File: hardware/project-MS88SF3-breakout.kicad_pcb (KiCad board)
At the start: 4 copper layers, 22.9 x 50.8 mm, 27 parts, among them J1 Conn_02x05_Odd_Even, J2 S2B-PH-SM4-TB(LF)(SN), J3 USB4105-GF-A, J4 Conn_01x12_Pin, J5 Conn_01x16_Pin, SW1 PTS810_SJM_250_SMTR_LFS, U1 MS88SF3_NRF52840

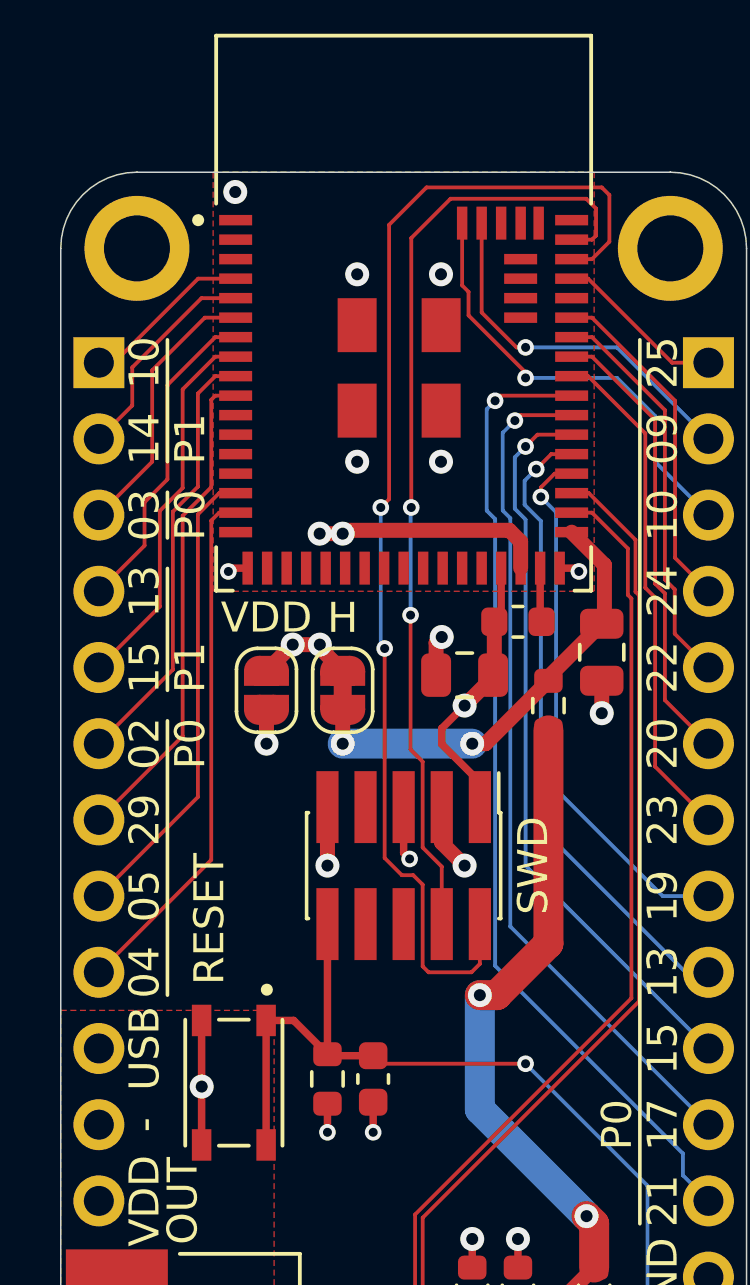
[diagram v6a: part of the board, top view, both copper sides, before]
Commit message: Route all nets
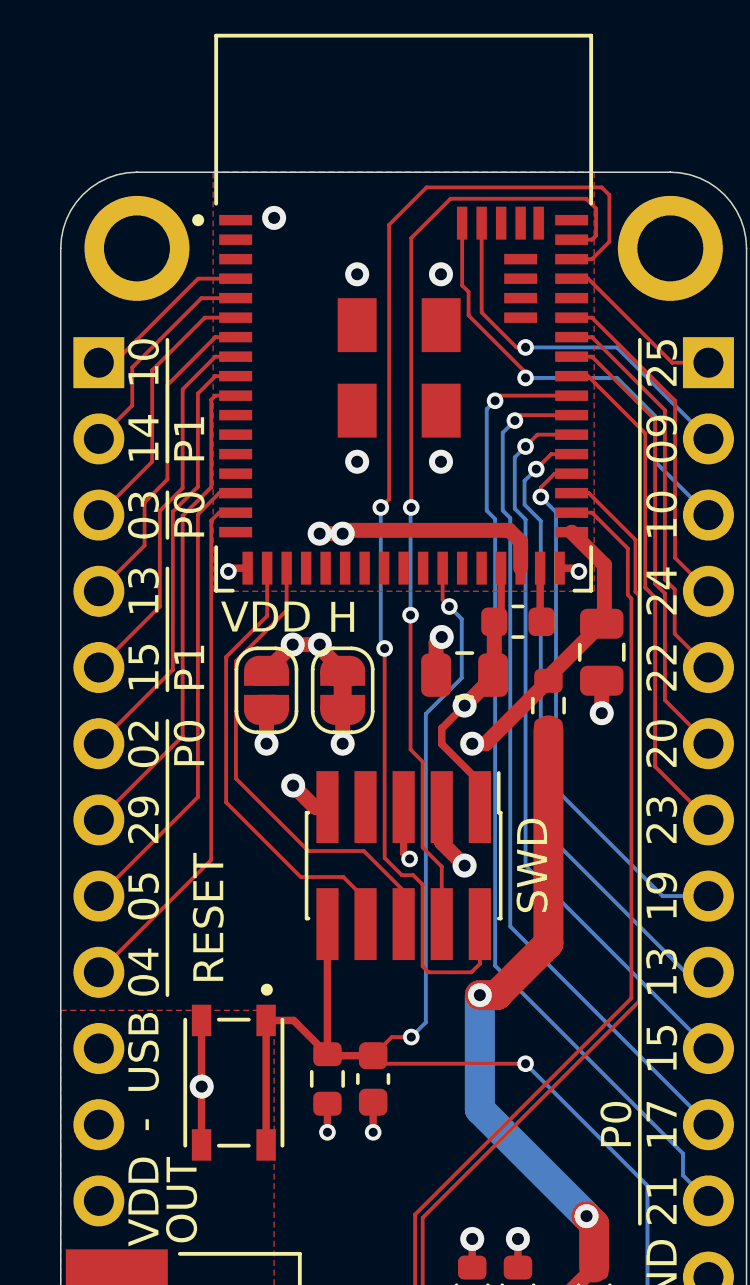
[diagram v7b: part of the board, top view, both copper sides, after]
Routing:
- net /RESET: track 35.0 -> 53.1 mm, vias 1 -> 3
- net /TX: track 0.00 -> 16.0 mm
- net /RX: track 0.00 -> 15.2 mm
- net GND: track 28.8 -> 28.2 mm
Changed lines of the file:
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@@
 	)
 	(gr_text "USB"
-		(at 38.862 109.982 90)
+		(at 38.862 110.109 90)
 		(layer "F.SilkS")
 		(effects
@@
 		(end 49.784048 99.822)
 		(width 1)
-		(layer "B.Cu")
+		(layer "In2.Cu")
 		(net 5)
 	)
@@
 	)
 	(segment
-		(start 44.958 101.936)
-		(end 44.958 103.886)
-		(width 0.5)
-		(layer "F.Cu")
-		(net 7)
-	)
-	(segment
 		(start 43.753 125.547)
 		(end 43.178 126.122)
@@
 	)
 	(segment
+		(start 44.958 101.936)
+		(end 44.532 101.936)
+		(width 0.5)
+		(layer "F.Cu")
+		(net 7)
+	)
+	(segment
 		(start 53.02 122.936)
 		(end 53.02 124.018)
@@
 	)
 	(segment
+		(start 44.532 101.936)
+		(end 43.815 101.219)
+		(width 0.5)
+		(layer "F.Cu")
+		(net 7)
+	)
+	(segment
 		(start 37.938 124.127)
 		(end 37.938 122.844)
@@
 	(via
 		(at 48.768 96.266)
+		(size 0.8)
+		(drill 0.4)
+		(layers "F.Cu" "B.Cu")
+		(net 7)
+	)
+	(via
+		(at 43.815 101.219)
 		(size 0.8)
 		(drill 0.4)
@@
 	)
 	(via
-		(at 41.8846 81.4324)
-		(size 0.8)
-		(drill 0.4)
-		(layers "F.Cu" "B.Cu")
-		(net 7)
-	)
-	(via
 		(at 48.7426 90.424)
 		(size 0.8)
@@
 	)
 	(via
-		(at 44.958 103.886)
-		(size 0.8)
-		(drill 0.4)
-		(layers "F.Cu" "B.Cu")
-		(net 7)
-	)
-	(via
 		(at 45.9486 90.424)
 		(size 0.8)
@@
 	)
 	(via
+		(at 43.18 82.296)
+		(size 0.8)
+		(drill 0.4)
+		(layers "F.Cu" "B.Cu")
+		(free yes)
+		(net 7)
+	)
+	(via
 		(at 38.1 122.682)
 		(size 0.8)
@@
 	)
 	(segment
+		(start 46.228 105.006)
+		(end 46.228 105.836)
+		(width 0.127)
+		(layer "F.Cu")
+		(net 16)
+	)
+	(segment
+		(start 41.5805 96.934795)
+		(end 41.5805 101.7785)
+		(width 0.127)
+		(layer "F.Cu")
+		(net 16)
+	)
+	(segment
+		(start 45.489 104.267)
+		(end 46.228 105.006)
+		(width 0.127)
+		(layer "F.Cu")
+		(net 16)
+	)
+	(segment
+		(start 44.069 104.267)
+		(end 45.489 104.267)
+		(width 0.127)
+		(layer "F.Cu")
+		(net 16)
+	)
+	(segment
+		(start 42.948 93.971)
+		(end 42.948 95.567295)
+		(width 0.127)
+		(layer "F.Cu")
+		(net 16)
+	)
+	(segment
+		(start 42.948 95.567295)
+		(end 41.5805 96.934795)
+		(width 0.127)
+		(layer "F.Cu")
+		(net 16)
+	)
+	(segment
+		(start 41.5805 101.7785)
+		(end 44.069 104.267)
+		(width 0.127)
+		(layer "F.Cu")
+		(net 16)
+	)
+	(segment
+		(start 41.9075 100.9825)
+		(end 44.3245 103.3995)
+		(width 0.127)
+		(layer "F.Cu")
+		(net 17)
+	)
+	(segment
+		(start 43.598 93.971)
+		(end 43.598 95.379743)
+		(width 0.127)
+		(layer "F.Cu")
+		(net 17)
+	)
+	(segment
+		(start 46.169948 103.3995)
+		(end 47.498 104.727552)
+		(width 0.127)
+		(layer "F.Cu")
+		(net 17)
+	)
+	(segment
+		(start 44.3245 103.3995)
+		(end 46.169948 103.3995)
+		(width 0.127)
+		(layer "F.Cu")
+		(net 17)
+	)
+	(segment
+		(start 43.598 95.379743)
+		(end 41.9075 97.070243)
+		(width 0.127)
+		(layer "F.Cu")
+		(net 17)
+	)
+	(segment
+		(start 47.498 104.727552)
+		(end 47.498 105.836)
+		(width 0.127)
+		(layer "F.Cu")
+		(net 17)
+	)
+	(segment
+		(start 41.9075 97.070243)
+		(end 41.9075 100.9825)
+		(width 0.127)
+		(layer "F.Cu")
+		(net 17)
+	)
+	(segment
+		(start 48.798 93.971)
+		(end 48.798 95.026)
+		(width 0.127)
+		(layer "F.Cu")
+		(net 20)
+	)
+	(segment
+		(start 48.798 95.026)
+		(end 49.022 95.25)
+		(width 0.127)
+		(layer "F.Cu")
+		(net 20)
+	)
+	(segment
 		(start 45.008 110.223)
 		(end 44.958 110.173)
@@
 	)
 	(segment
+		(start 46.482 110.223)
+		(end 47.104 109.601)
+		(width 0.127)
+		(layer "F.Cu")
+		(net 20)
+	)
+	(segment
 		(start 42.913 113.197)
 		(end 42.913 109.047)
 		(width 0.25)
 		(layer "F.Cu")
+		(net 20)
+	)
+	(segment
+		(start 47.104 109.601)
+		(end 47.752 109.601)
+		(width 0.127)
+		(layer "F.Cu")
+		(net 20)
+	)
+	(via
+		(at 47.752 109.601)
+		(size 0.554)
+		(drill 0.3)
+		(layers "F.Cu" "B.Cu")
+		(net 20)
+	)
+	(via
+		(at 49.022 95.25)
+		(size 0.554)
+		(drill 0.3)
+		(layers "F.Cu" "B.Cu")
 		(net 20)
 	)
@@
 	)
 	(segment
+		(start 49.4315 97.6345)
+		(end 48.23737 98.82863)
+		(width 0.127)
+		(layer "B.Cu")
+		(net 20)
+	)
+	(segment
 		(start 55.626 123.19)
 		(end 55.626 114.554)
@@
 	)
 	(segment
+		(start 49.022 95.25)
+		(end 49.4315 95.6595)
+		(width 0.127)
+		(layer "B.Cu")
+		(net 20)
+	)
+	(segment
+		(start 48.23737 109.11563)
+		(end 47.752 109.601)
+		(width 0.127)
+		(layer "B.Cu")
+		(net 20)
+	)
+	(segment
+		(start 49.4315 95.6595)
+		(end 49.4315 97.6345)
+		(width 0.127)
+		(layer "B.Cu")
+		(net 20)
+	)
+	(segment
 		(start 55.626 114.554)
 		(end 51.562 110.49)
 		(width 0.127)
 		(layer "B.Cu")
+		(net 20)
+	)
+	(segment
+		(start 48.23737 98.82863)
+		(end 48.23737 109.11563)
+		(width 0.127)
+		(layer "B.Cu")

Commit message: Bring back the panda
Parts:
- added Ref**: Val**, drawing:bear-body_silk_16x16, B.Cu at (45.6, 121.0)
